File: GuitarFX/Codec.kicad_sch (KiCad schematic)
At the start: 1 part, among them U1 CS4272

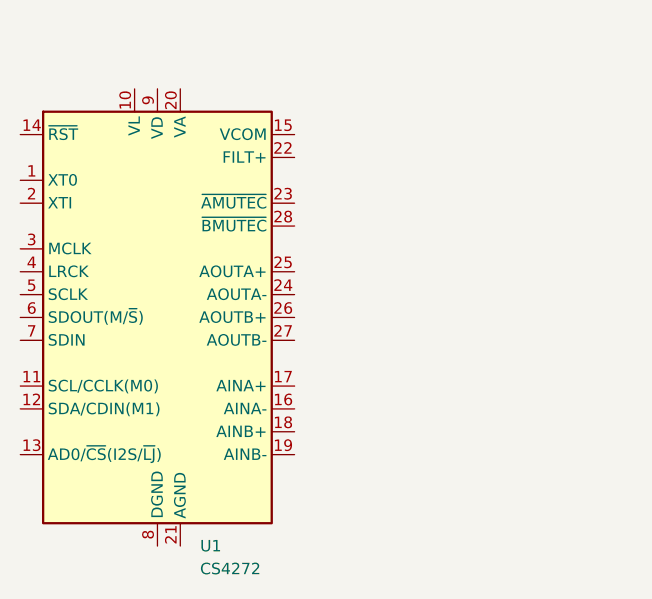
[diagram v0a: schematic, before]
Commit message: Finished tag connect SWD connections on schematic
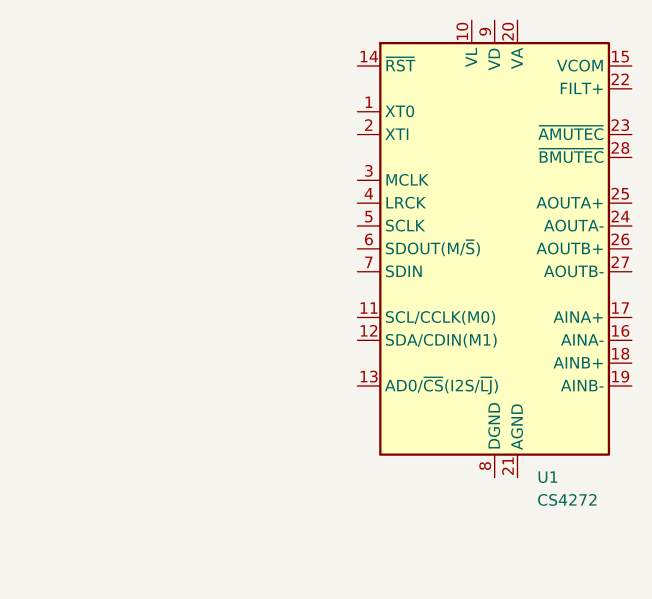
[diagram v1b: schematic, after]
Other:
- moved on the sheet: U1
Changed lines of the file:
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@@
 (kicad_sch (version 20230121) (generator eeschema)
   (paper "A4")
-  (symbol (lib_id "Audio:CS4272") (at 71.755 90.17 0) (unit 1)
+  (symbol (lib_id "Audio:CS4272") (at 109.22 82.55 0) (unit 1)
     (in_bom yes) (on_board yes) (dnp no) (fields_autoplaced)
-    (property "Reference" "U1" (at 76.4891 115.57 0)
+    (property "Reference" "U1" (at 113.9541 107.95 0)
       (effects (font (size 1.27 1.27)) (justify left))
     )
-    (property "Value" "CS4272" (at 76.4891 118.11 0)
+    (property "Value" "CS4272" (at 113.9541 110.49 0)
       (effects (font (size 1.27 1.27)) (justify left))
     )
-    (property "Footprint" "Package_SO:TSSOP-28_4.4x9.7mm_P0.65mm" (at 71.755 90.17 0)
+    (property "Footprint" "Package_SO:TSSOP-28_4.4x9.7mm_P0.65mm" (at 109.22 82.55 0)
       (effects (font (size 1.27 1.27)) hide)
     )
-    (property "Datasheet" "https://statics.cirrus.com/pubs/proDatasheet/CS4272_F1.pdf" (at 71.755 90.17 0)
+    (property "Datasheet" "https://statics.cirrus.com/pubs/proDatasheet/CS4272_F1.pdf" (at 109.22 82.55 0)
       (effects (font (size 1.27 1.27)) hide)
     )

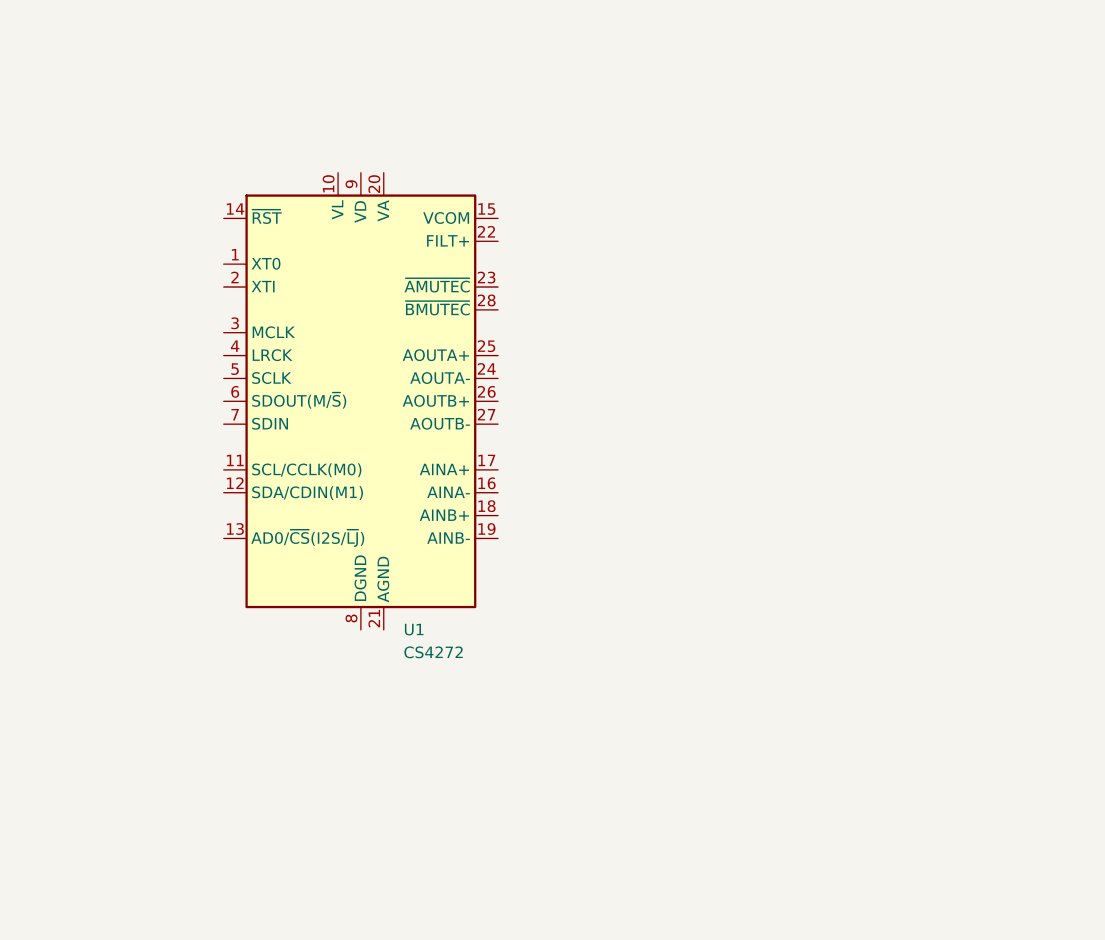
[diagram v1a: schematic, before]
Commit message: Added decoupling caps to codec
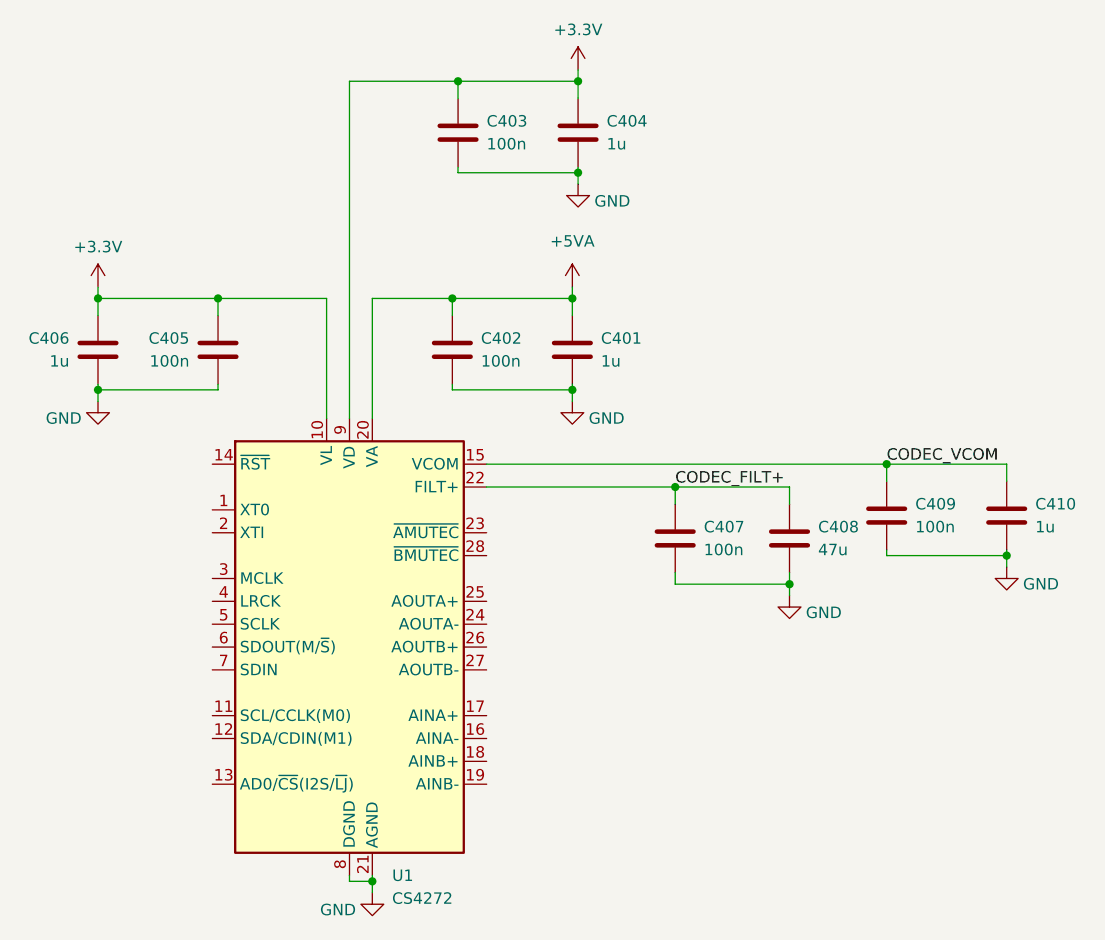
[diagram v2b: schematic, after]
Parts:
- added C401, C404, C406, C410: 1u, symbol Device:C
- added C402, C403, C405, C407, C409: 100n, symbol Device:C
- added C408: 47u, symbol Device:C
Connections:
- net +3.3V: now reaches U1.10 (VL)
- net +3.3V: now also U1.9 (VD), C403.1, C404.1, C405.1, C406.1
- net CODEC_VCOM: now reaches U1.15 (VCOM)
- net CODEC_VCOM: now also C409.1, C410.1
- net +5VA: now reaches U1.20 (VA)
- net +5VA: now also C401.1, C402.1
- net GND: now reaches U1.21 (AGND)
- net GND: now also U1.8 (DGND), C401.2, C402.2, C403.2, C404.2, C405.2, C406.2, C407.2, C408.2, C409.2, C410.2
- net CODEC_FILT+: now reaches U1.22 (FILT+)
- net CODEC_FILT+: now also C407.1, C408.1
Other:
- moved on the sheet: U1

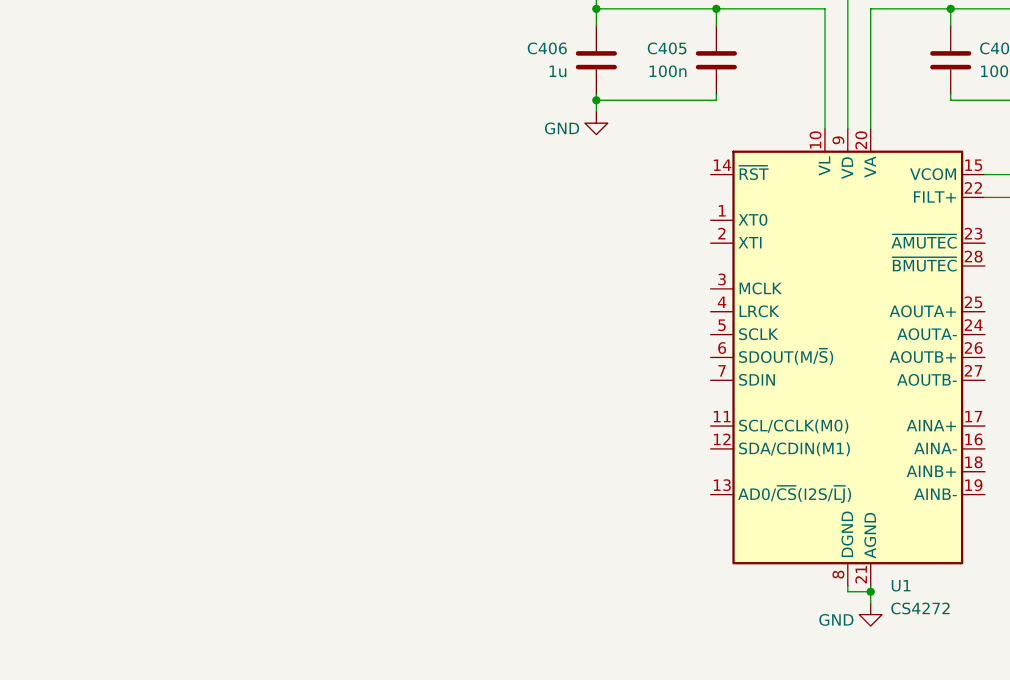
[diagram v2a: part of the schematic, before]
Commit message: Finished i2s and i2c connections on codec and mcu
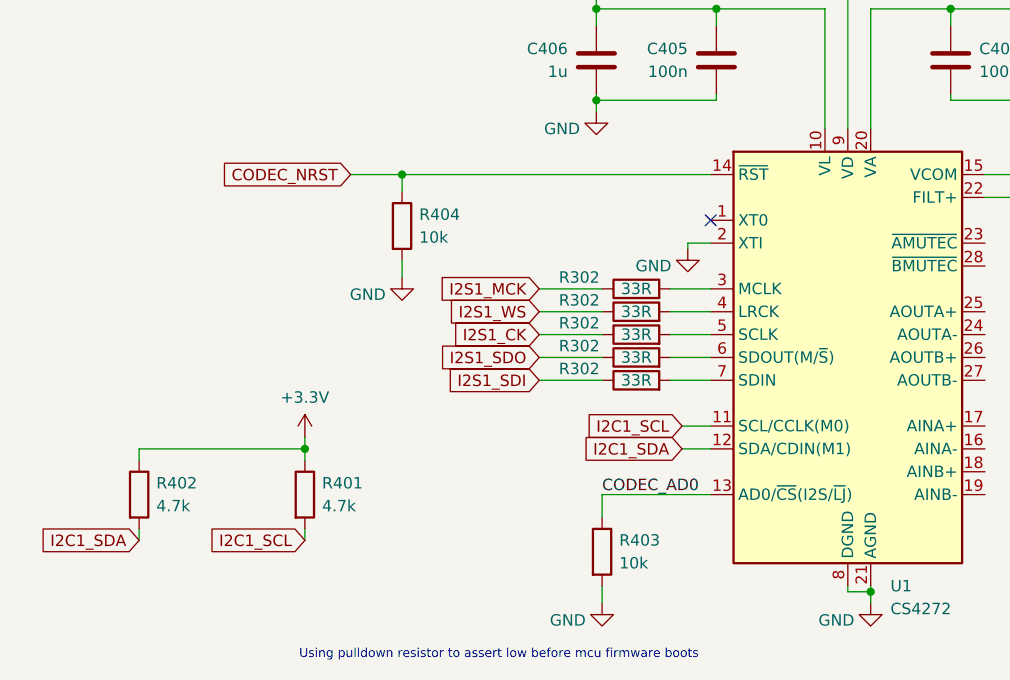
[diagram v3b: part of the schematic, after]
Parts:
- added R302 (x5): 33R, symbol Device:R
- added R401, R402: 4.7k, symbol Device:R
- added R403, R404: 10k, symbol Device:R
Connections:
- net +3.3V: now also R401.1, R402.1
- net GND: now also U1.2 (XTI), R403.2, R404.2
- net I2C1_SCL: now reaches U1.11 (SCL/CCLK(M0))
- net I2C1_SCL: now also R401.2
- net I2C1_SDA: now reaches U1.12 (SDA/CDIN(M1))
- net I2C1_SDA: now also R402.2
- net CODEC_AD0: now reaches U1.13 (AD0/~{CS}(I2S/~{LJ}))
- net CODEC_AD0: now also R403.1
- net CODEC_NRST: now reaches U1.14 (~{RST})
- net CODEC_NRST: now also R404.1
- net at U1.3 (MCLK): now also R302.2
- net at U1.4 (LRCK): now also R302.2
- net at U1.5 (SCLK): now also R302.2
- net at U1.6 (SDOUT(M/~{S})): now also R302.2
- net at U1.7 (SDIN): now also R302.2
- new net I2S1_CK: R302.1
- new net I2S1_MCK: R302.1
- new net I2S1_SDI: R302.1
- new net I2S1_SDO: R302.1
- new net I2S1_WS: R302.1
- no-connect marks 0 -> 1
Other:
- note added: "Using pulldown resistor to assert low before mcu firmware boots"

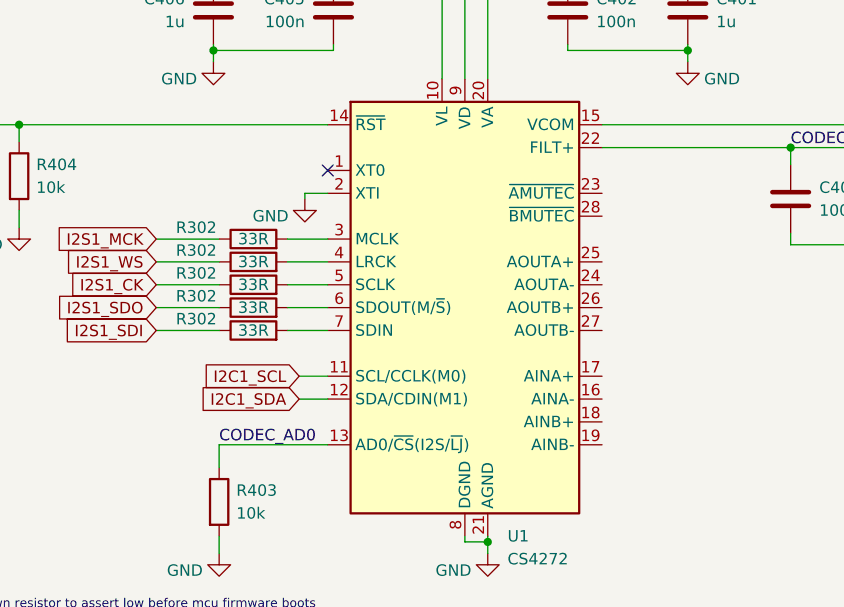
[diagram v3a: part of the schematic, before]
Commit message: Added new codec: PCM3060
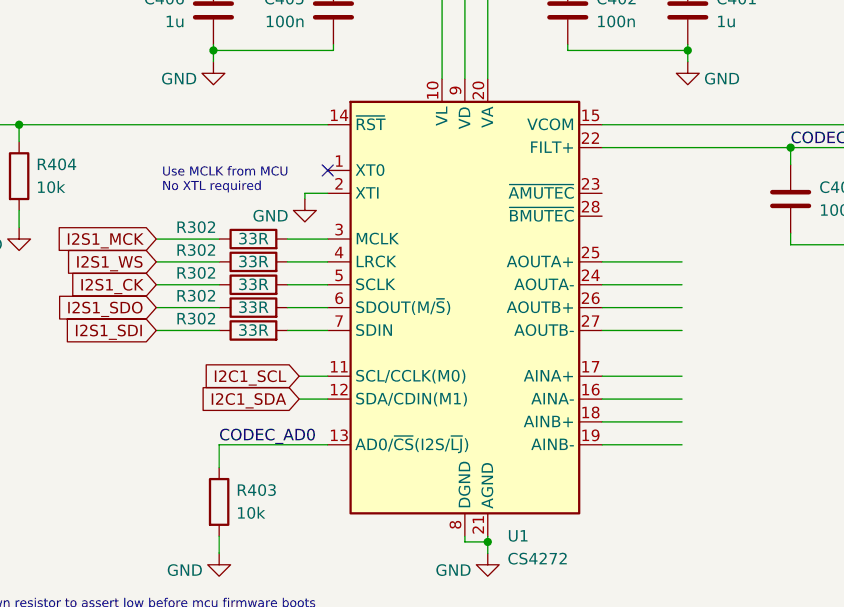
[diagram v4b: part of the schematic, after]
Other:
- note added: "Use MCLK from MCU No XTL required"
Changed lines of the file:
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@@
   )
   (no_connect (at 92.71 94.615))
+  (wire (pts (xy 123.19 107.315) (xy 132.08 107.315))
+    (stroke (width 0) (type default))
+  )
   (wire (pts (xy 80.645 125.095) (xy 80.645 127.635))
     (stroke (width 0) (type default))
@@
     (stroke (width 0) (type default))
   )
+  (wire (pts (xy 123.19 122.555) (xy 132.08 122.555))
+    (stroke (width 0) (type default))
+  )
   (wire (pts (xy 73.66 102.235) (xy 80.645 102.235))
     (stroke (width 0) (type default))
@@
     (stroke (width 0) (type default))
   )
+  (wire (pts (xy 123.19 120.015) (xy 132.08 120.015))
+    (stroke (width 0) (type default))
+  )
   (wire (pts (xy 156.845 102.87) (xy 156.845 101.6))
     (stroke (width 0) (type default))
@@
     (stroke (width 0) (type default))
   )
+  (wire (pts (xy 123.19 117.475) (xy 132.08 117.475))
+    (stroke (width 0) (type default))
+  )
   (wire (pts (xy 107.95 135.89) (xy 110.49 135.89))
     (stroke (width 0) (type default))
@@
     (stroke (width 0) (type default))
   )
+  (wire (pts (xy 123.19 109.855) (xy 132.08 109.855))
+    (stroke (width 0) (type default))
+  )
   (wire (pts (xy 73.66 107.315) (xy 80.645 107.315))
     (stroke (width 0) (type default))
@@
     (stroke (width 0) (type default))
   )
+  (wire (pts (xy 123.19 125.095) (xy 132.08 125.095))
+    (stroke (width 0) (type default))
+  )
   (wire (pts (xy 107.95 135.255) (xy 107.95 135.89))
     (stroke (width 0) (type default))
   )
+  (wire (pts (xy 123.19 112.395) (xy 132.08 112.395))
+    (stroke (width 0) (type default))
+  )
   (wire (pts (xy 89.535 117.475) (xy 92.71 117.475))
     (stroke (width 0) (type default))
@@
     (stroke (width 0) (type default))
   )
+  (wire (pts (xy 123.19 104.775) (xy 132.08 104.775))
+    (stroke (width 0) (type default))
+  )
   (wire (pts (xy 88.265 109.855) (xy 92.71 109.855))
     (stroke (width 0) (type default))
   )
+  (text "Use MCLK from MCU \nNo XTL required" (at 74.295 97.155 0)
+    (effects (font (size 1 1)) (justify left bottom))
+  )
   (text "Using pulldown resistor to assert low before mcu firmware boots"

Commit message: Added connections to CODEC
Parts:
- added C411, C414, C415: 10u, symbol Device:C
- added C412, C413, C416: 0.1u, symbol Device:C
- added IC401: PCM3060PWR, SOP65P640X120-28N, symbol PCM3060PWR:PCM3060PWR
- added R302 (x5): 33R, symbol Device:R
- added R410: 10k, symbol Device:R
- added R415, R416: 4.7k, symbol Device:R
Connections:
- net +3.3V: now also C413.1, C414.1, IC401.7 (VDD), R415.1, R416.1
- net +5VA: now also C411.1, C412.1, IC401.24 (VCC)
- net CODEC_NRST: now also IC401.15 (~{RST}), R410.1
- net CODEC_VCOM: now also C415.1, C416.1, IC401.21 (VCOM)
- net GND: now also C411.2, C412.2, C413.2, C414.2, C415.2, C416.2, IC401.16 (SGND), IC401.22 (AGND2), IC401.23 (AGND1), IC401.27 (~{MS}/ADR/IFMD), IC401.28 (MODE), IC401.8 (DGND), R410.2
- net I2C1_SCL: now also IC401.1 (MC/SCL/FMT), R416.2
- net I2C1_SDA: now also IC401.2 (MD/SDA/DEMP), R415.2
- net I2S1_CK: now also R302.1
- net I2S1_MCK: now also R302.1
- net I2S1_SDI: now also R302.1
- net I2S1_SDO: now also R302.1
- net I2S1_WS: now also R302.1
- new net: IC401.3 (DOUT), R302.2
- new net: IC401.5 (BCK1), R302.2
- new net: IC401.12 (DIN), R302.2
- new net: IC401.4 (LRCK1), R302.2
- new net: IC401.6 (SCKI1), R302.2
- new net CODEC_VINL: IC401.25 (VINL)
- new net CODEC_VINR: IC401.26 (VINR)
- new net CODEC_VOUTL: IC401.20 (VOUTL+)
- new net CODEC_VOUTR: IC401.18 (VOUTR+)
- no-connect marks 1 -> 8
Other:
- note added: "GND configures I2C mode"
- note added: "GND configures LSB of I2C address to be 0"
- moved on the sheet: C401, C402, C403, C404, C405, C406, C407, C408, C409, C410, R302, R401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
